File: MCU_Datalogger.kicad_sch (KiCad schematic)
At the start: 25 parts, among them U1 24LC1025, U2 24LC1025, U3 DS1337S_, U4 ATMEGA328P-AN, Y1 Crystal, Y2 Crystal

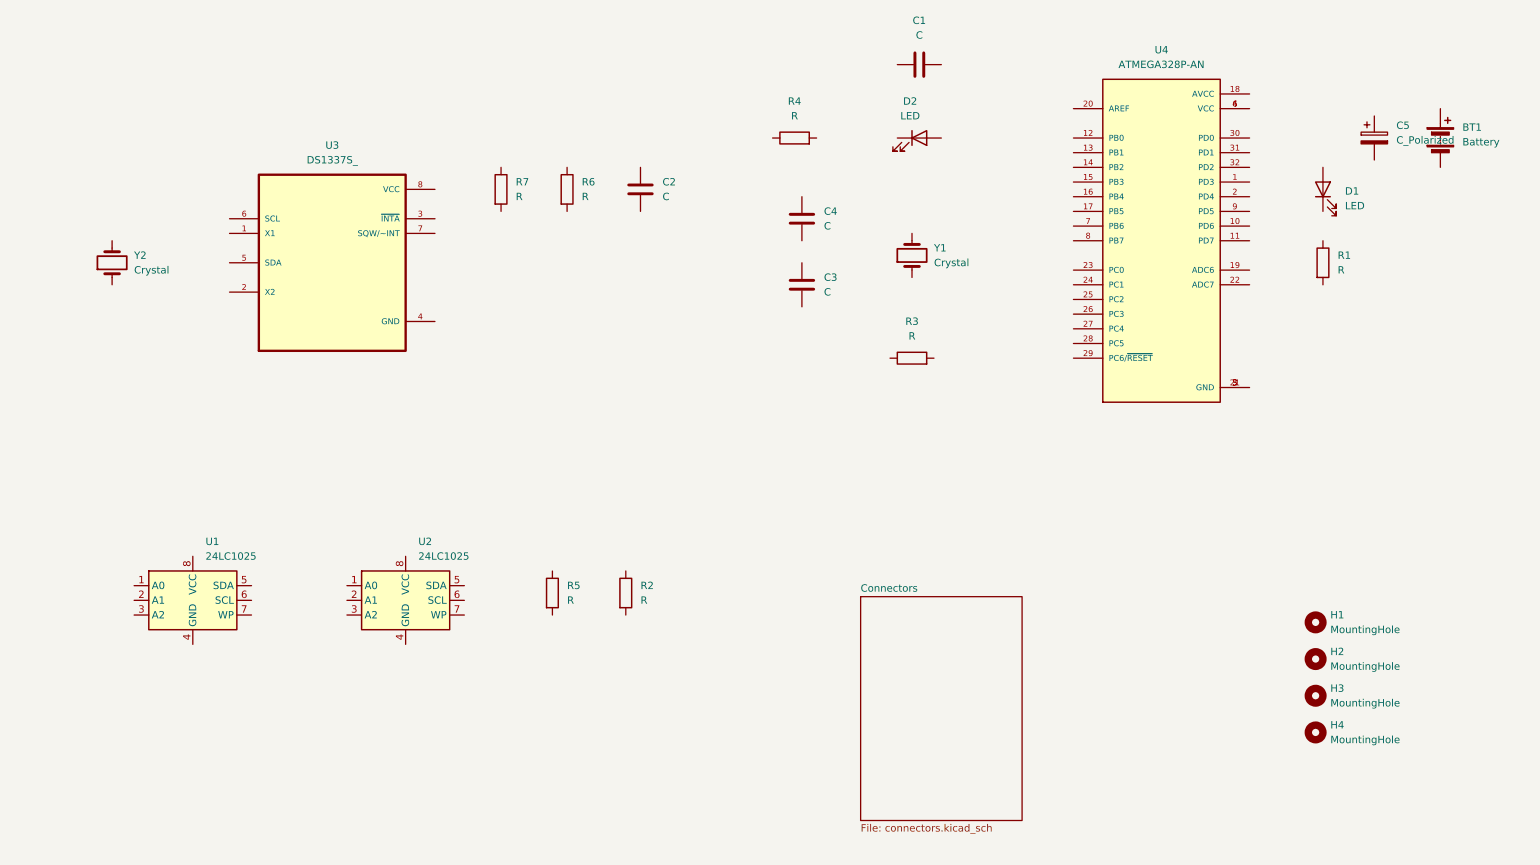
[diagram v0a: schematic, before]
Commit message: Added Component Values.
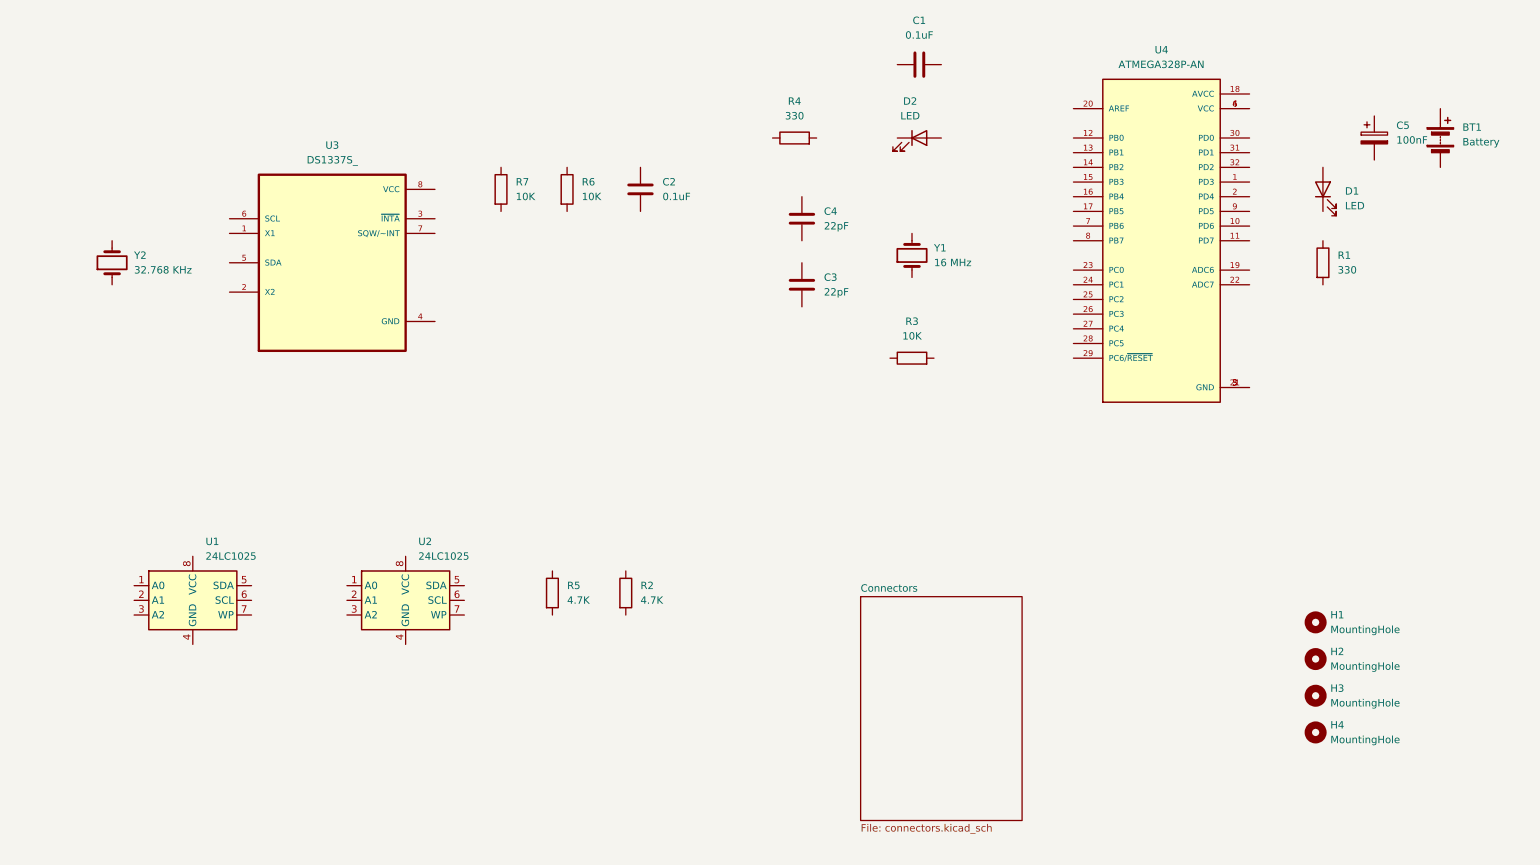
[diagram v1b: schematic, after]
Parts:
- C1, C2: value C -> 0.1uF
- C3, C4: value C -> 22pF
- C5: value C_Polarized -> 100nF
- R1, R4: value R -> 330
- R2, R5: value R -> 4.7K
- R3, R6, R7: value R -> 10K
- Y1: value Crystal -> 16 MHz
- Y2: value Crystal -> 32.768 KHz
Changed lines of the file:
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@@
 			)
 		)
-		(property "Value" "Crystal"
+		(property "Value" "16 MHz"
 			(at 179.07 59.6899 90)
 			(effects
@@
 			)
 		)
-		(property "Value" "C"
+		(property "Value" "0.1uF"
 			(at 132.08 48.2599 0)
 			(effects
@@
 			)
 		)
+		(property "Purpose" ""
+			(at 128.27 46.99 0)
+			(effects
+				(font
+					(size 1.27 1.27)
+				)
+			)
+		)
 		(pin "1"
 		)
@@
 			)
 		)
-		(property "Value" "C"
+		(property "Value" "22pF"
 			(at 160.02 64.7699 0)
 			(effects
@@
 			)
 		)
-		(property "Value" "Crystal"
+		(property "Value" "32.768 KHz"
 			(at 40.64 60.9599 90)
 			(effects
@@
 			)
 		)
+		(property "Purpose" ""
+			(at 36.83 59.69 0)
+			(effects
+				(font
+					(size 1.27 1.27)
+				)
+			)
+		)
 		(pin "1"
 		)
@@
 			)
 		)
-		(property "Value" "R"
+		(property "Value" "4.7K"
 			(at 128.27 118.1099 0)
 			(effects
@@
 			)
 		)
-		(property "Value" "R"
+		(property "Value" "330"
 			(at 248.92 60.9599 0)
 			(effects
@@
 			)
 		)
+		(property "Purpose" ""
+			(at 246.38 59.69 0)
+			(effects
+				(font
+					(size 1.27 1.27)
+				)
+			)
+		)
 		(pin "2"
 		)
@@
 			)
 		)
-		(property "Value" "C_Polarized"
+		(property "Value" "100nF"
 			(at 259.08 38.4809 0)
 			(effects
@@
 			)
 		)
+		(property "Purpose" ""
+			(at 255.27 38.1 0)
+			(effects
+				(font
+					(size 1.27 1.27)
+				)
+			)
+		)
 		(pin "2"
 		)
@@
 			)
 		)
-		(property "Value" "R"
+		(property "Value" "330"
 			(at 154.94 34.29 90)
 			(effects
@@
 			)
 		)
+		(property "Purpose" ""
+			(at 154.94 38.1 0)
+			(effects
+				(font
+					(size 1.27 1.27)
+				)
+			)
+		)
 		(pin "2"
 		)
@@
 			)
 		)
-		(property "Value" "R"
+		(property "Value" "10K"
 			(at 106.68 48.2599 0)
 			(effects
@@
 			)
 		)
+		(property "Purpose" ""
+			(at 104.14 46.99 0)
+			(effects
+				(font
+					(size 1.27 1.27)
+				)
+			)
+		)
 		(pin "2"
 		)
@@
 			)
 		)
-		(property "Value" "R"
+		(property "Value" "4.7K"
 			(at 115.57 118.1099 0)
 			(effects
@@
 			)
 		)
+		(property "Purpose" ""
+			(at 113.03 116.84 0)
+			(effects
+				(font
+					(size 1.27 1.27)
+				)
+			)
+		)
 		(pin "2"
 		)
@@
 			)
 		)
-		(property "Value" "R"
+		(property "Value" "10K"
 			(at 175.26 72.39 90)
 			(effects
@@
 			)
 		)
+		(property "Purpose" ""
+			(at 175.26 76.2 0)
+			(effects
+				(font
+					(size 1.27 1.27)
+				)
+			)
+		)
 		(pin "2"
 		)
@@
 			)
 		)
-		(property "Value" "C"
+		(property "Value" "22pF"
 			(at 160.02 53.3399 0)
 			(effects
@@
 			)
 		)
-		(property "Value" "R"
+		(property "Value" "10K"
 			(at 118.11 48.2599 0)
 			(effects
@@
 			)
 		)
+		(property "Purpose" ""
+			(at 115.57 46.99 0)
+			(effects
+				(font
+					(size 1.27 1.27)
+				)
+			)
+		)
 		(pin "2"
 		)
@@
 			)
 		)
-		(property "Value" "C"
+		(property "Value" "0.1uF"
 			(at 176.53 20.32 90)
 			(effects
@@
 			)
 		)
+		(property "Purpose" ""
+			(at 176.53 25.4 0)
+			(effects
+				(font
+					(size 1.27 1.27)
+				)
+			)
+		)

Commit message: Assigned Footprints.
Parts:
- BT1: footprint (none) -> Connector_PinHeader_2.54mm:PinHeader_1x02_P2.54mm_Vertical
- C1, C2, C3, C4, C5: footprint (none) -> Capacitor_SMD:C_0805_2012Metric
- D1, D2: footprint (none) -> LED_SMD:LED_0805_2012Metric
- H1, H2, H3, H4: footprint (none) -> MountingHole:MountingHole_2.1mm
- R1, R2, R3, R4, R5, R6, R7: footprint (none) -> Resistor_SMD:R_0805_2012Metric
- U1, U2: footprint (none) -> Package_SO:SOIC-8_5.23x5.23mm_P1.27mm
- U3: footprint DS1337S_:SOIC127P600X175-8N -> footprints:SOIC127P600X175-8N
- U4: footprint ATMEGA328P-AN:QFP80P900X900X120-32N -> footprints:QFP80P900X900X120-32N
- Y1, Y2: footprint (none) -> Crystal:Crystal_SMD_5032-2Pin_5.0x3.2mm_HandSoldering
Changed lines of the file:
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@@
 			)
 		)
-		(property "Footprint" ""
+		(property "Footprint" "Crystal:Crystal_SMD_5032-2Pin_5.0x3.2mm_HandSoldering"
 			(at 175.26 58.42 0)
 			(effects
@@
 			)
 		)
-		(property "Footprint" ""
+		(property "Footprint" "Capacitor_SMD:C_0805_2012Metric"
 			(at 129.2352 50.8 0)
 			(effects
@@
 			)
 		)
-		(property "Footprint" ""
+		(property "Footprint" "Capacitor_SMD:C_0805_2012Metric"
 			(at 157.1752 67.31 0)
 			(effects
@@
 			)
 		)
-		(property "Footprint" ""
+		(property "Footprint" "Crystal:Crystal_SMD_5032-2Pin_5.0x3.2mm_HandSoldering"
 			(at 36.83 59.69 0)
 			(effects
@@
 			)
 		)
-		(property "Footprint" ""
+		(property "Footprint" "LED_SMD:LED_0805_2012Metric"
 			(at 176.53 38.1 0)
 			(effects
@@
 			)
 		)
-		(property "Footprint" "ATMEGA328P-AN:QFP80P900X900X120-32N"
+		(property "Footprint" "footprints:QFP80P900X900X120-32N"
 			(at 218.44 55.88 0)
 			(effects
@@
 			)
 		)
-		(property "Footprint" ""
+		(property "Footprint" "Resistor_SMD:R_0805_2012Metric"
 			(at 123.952 116.84 90)
 			(effects
@@
 			)
 		)
-		(property "Footprint" ""
+		(property "Footprint" "Resistor_SMD:R_0805_2012Metric"
 			(at 244.602 59.69 90)
 			(effects
@@
 			)
 		)
-		(property "Footprint" ""
+		(property "Footprint" "MountingHole:MountingHole_2.1mm"
 			(at 245.11 140.97 0)
 			(effects
@@
 			)
 		)
-		(property "Footprint" ""
+		(property "Footprint" "Package_SO:SOIC-8_5.23x5.23mm_P1.27mm"
 			(at 87.63 118.11 0)
 			(effects
@@
 			)
 		)
-		(property "Footprint" ""
+		(property "Footprint" "MountingHole:MountingHole_2.1mm"
 			(at 245.11 134.62 0)
 			(effects
@@
 			)
 		)
-		(property "Footprint" ""
+		(property "Footprint" "Package_SO:SOIC-8_5.23x5.23mm_P1.27mm"
 			(at 50.8 118.11 0)
 			(effects
@@
 			)
 		)
-		(property "Footprint" ""
+		(property "Footprint" "LED_SMD:LED_0805_2012Metric"
 			(at 246.38 46.99 0)
 			(effects
@@
 			)
 		)
-		(property "Footprint" ""
+		(property "Footprint" "Capacitor_SMD:C_0805_2012Metric"
 			(at 256.2352 41.91 0)
 			(effects
@@
 			)
 		)
-		(property "Footprint" "DS1337S_:SOIC127P600X175-8N"
+		(property "Footprint" "footprints:SOIC127P600X175-8N"
 			(at 74.93 59.69 0)
 			(effects
@@
 			)
 		)
-		(property "Footprint" ""
+		(property "Footprint" "Resistor_SMD:R_0805_2012Metric"
 			(at 154.94 39.878 90)
 			(effects
@@
 			)
 		)
-		(property "Footprint" ""
+		(property "Footprint" "Resistor_SMD:R_0805_2012Metric"
 			(at 102.362 46.99 90)
 			(effects
@@
 			)
 		)
-		(property "Footprint" ""
+		(property "Footprint" "Resistor_SMD:R_0805_2012Metric"
 			(at 111.252 116.84 90)
 			(effects
@@
 			)
 		)
-		(property "Footprint" ""
+		(property "Footprint" "Resistor_SMD:R_0805_2012Metric"
 			(at 175.26 77.978 90)
 			(effects
@@
 			)
 		)
-		(property "Footprint" ""
+		(property "Footprint" "Connector_PinHeader_2.54mm:PinHeader_1x02_P2.54mm_Vertical"
 			(at 266.7 36.576 90)
 			(effects
@@
 			)
 		)
-		(property "Footprint" ""
+		(property "Footprint" "MountingHole:MountingHole_2.1mm"
 			(at 245.11 128.27 0)
 			(effects
@@
 			)
 		)
-		(property "Footprint" ""
+		(property "Footprint" "Capacitor_SMD:C_0805_2012Metric"
 			(at 157.1752 55.88 0)
 			(effects
@@
 			)
 		)
-		(property "Footprint" ""
+		(property "Footprint" "Resistor_SMD:R_0805_2012Metric"
 			(at 113.792 46.99 90)
 			(effects
@@
 			)
 		)
-		(property "Footprint" ""
+		(property "Footprint" "MountingHole:MountingHole_2.1mm"
 			(at 245.11 121.92 0)
 			(effects
@@
 			)
 		)
-		(property "Footprint" ""
+		(property "Footprint" "Capacitor_SMD:C_0805_2012Metric"
 			(at 180.34 24.4348 0)
 			(effects

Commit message: Finished Wiring of Main Sheet.
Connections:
- net at Y1.1: now also C3.2, U4.8 (PB7)
- net at Y1.2: now also C4.2, U4.7 (PB6)
- net Vcc: now reaches C2.1
- net Vcc: now also R2.1, R3.1, R5.1, R6.1, R7.1, U1.1 (A0), U1.2 (A1), U1.3 (A2), U1.8 (VCC), U2.1 (A0), U2.3 (A2), U2.8 (VCC), U3.8 (VCC)
- net GND: now reaches C2.2
- net GND: now also BT1.2 (-), C1.1, C3.1, C4.1, C5.2, R1.2, R4.1, U1.4 (GND), U1.7 (WP), U2.2 (A1), U2.4 (GND), U2.7 (WP), U3.4 (GND), U4.21 (GND), U4.3 (GND), U4.5 (GND)
- net at Y2.1: now also U3.2 (X2)
- net at Y2.2: now also U3.1 (X1)
- net at D2.1 (K): now also R4.2
- net SCK: now reaches D2.2 (A)
- net SCK: now also R5.2, U1.6 (SCL), U2.6 (SCL), U3.6 (SCL), U4.17 (PB5), U4.28 (PC5)
- net D3: now reaches U4.1 (PD3)
- net D6: now reaches U4.10 (PD6)
- net D7: now reaches U4.11 (PD7)
- net D8: now reaches U4.12 (PB0)
- net MOSI: now reaches U4.15 (PB3)
- net MISO: now reaches U4.16 (PB4)
- net at U4.18 (AVCC): now also BT1.1 (+), C5.1, D1.2 (A), U4.4 (VCC)
- net D4: now reaches U4.2 (PD4)
- net at U4.20 (AREF): now also C1.2
- net SDA: now reaches U4.27 (PC4)
- net SDA: now also R2.2, U1.5 (SDA), U2.5 (SDA), U3.5 (SDA)
- net RESET: now reaches U4.29 (PC6/~{RESET})
- net RESET: now also R3.2
- net RX: now reaches U4.30 (PD0)
- net TX: now reaches U4.31 (PD1)
- net D2: now reaches U4.32 (PD2)
- net at U4.6 (VCC): no longer U4.4 (VCC)
- net D5: now reaches U4.9 (PD5)
- net at R1.1: now also D1.1 (K)
- net at U3.3 (~{INTA}): now also R7.2
- net at U3.7 (SQW/~INT): now also R6.2
- no-connect marks 0 -> 9
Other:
- moved on the sheet: BT1, C1, C2, C3, C4, C5, D1, D2, R1, R2, R3, R4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

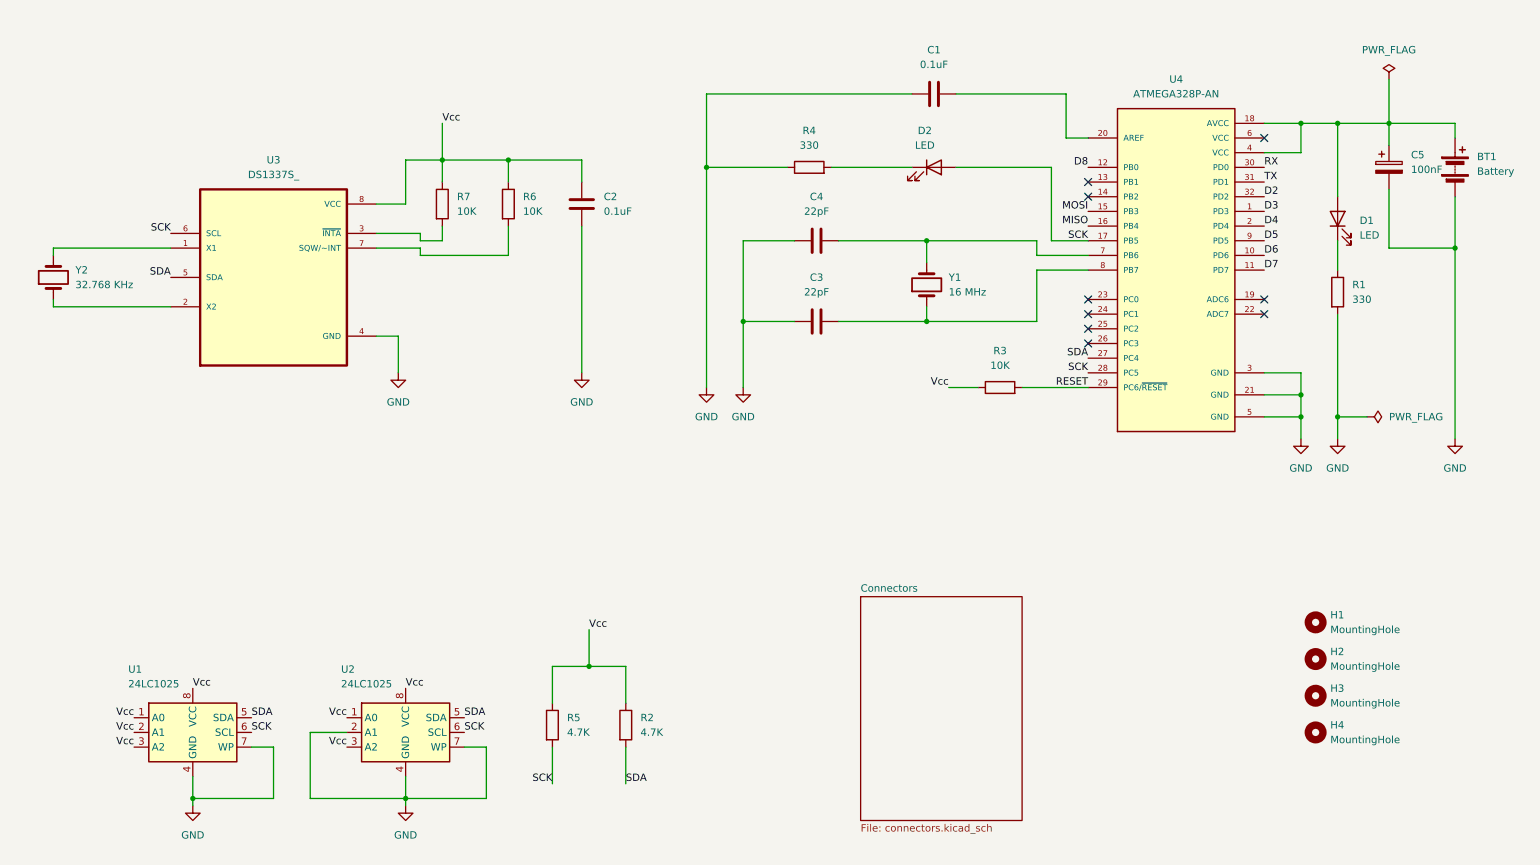
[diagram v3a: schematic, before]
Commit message: Completed Wiring in second sheet.
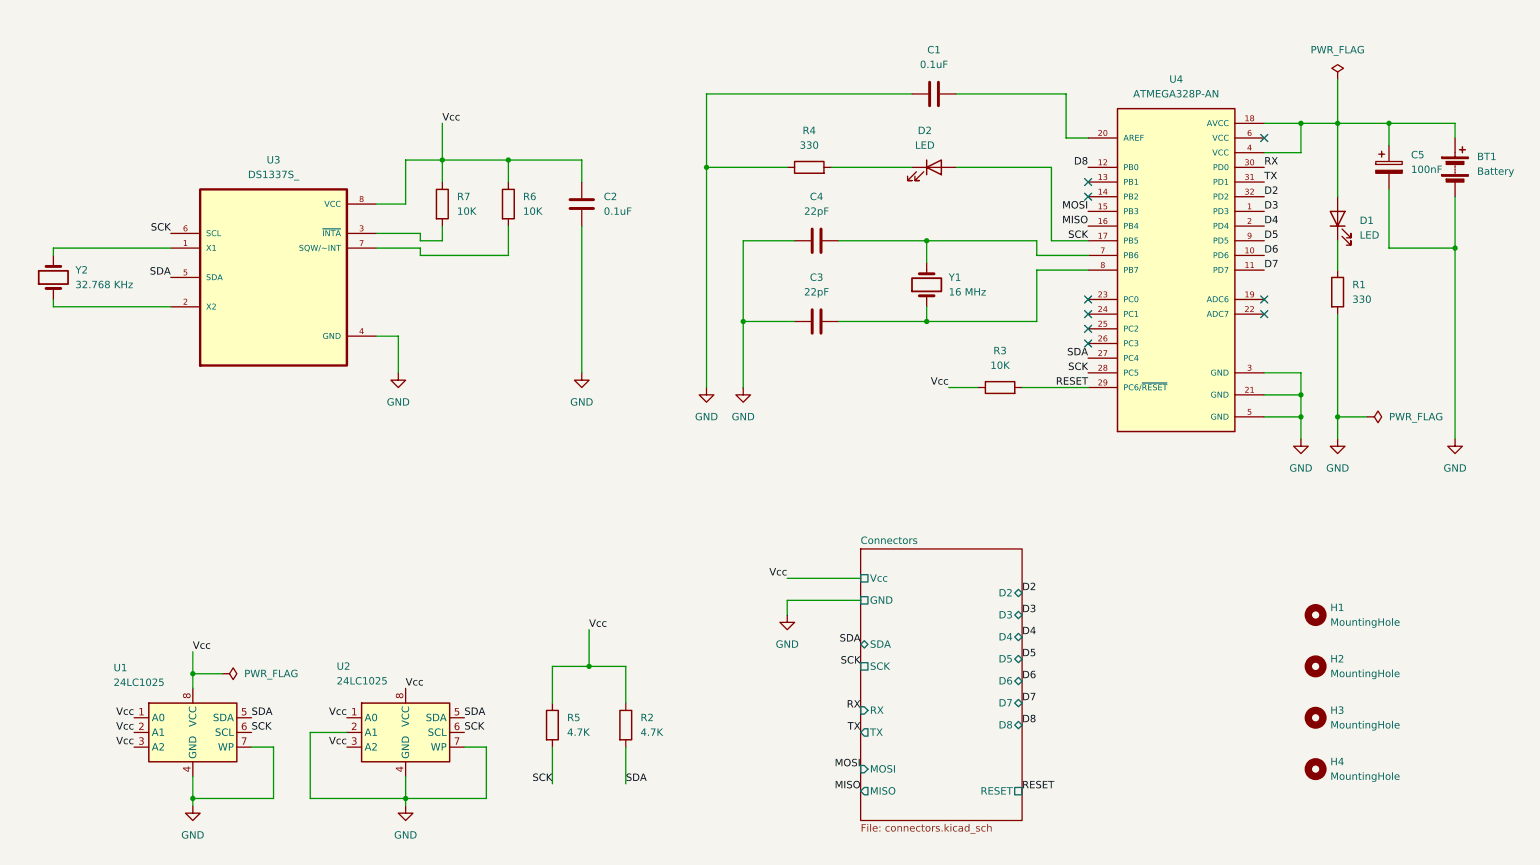
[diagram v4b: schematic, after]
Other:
- sheet Connectors ports: added D2, D3, D4, D5, D6, D7, D8, GND, MISO, MOSI, RESET, RX, SCK, SDA, TX, Vcc; removed none
- moved on the sheet: H1, H2, H3, H4
